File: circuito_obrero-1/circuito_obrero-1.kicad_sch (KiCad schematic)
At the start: 37 parts, among them J1 Conn_01x03_Pin, J10 Conn_01x05, J2 Conn_01x03_Pin, J3 Conn_01x03_Pin, J4 Conn_01x03_Pin, J5 Conn_01x03_Pin, J6 Conn_01x03_Pin, J7 Conn_01x03_Pin, J8 Conn_01x03_Pin, J9 Conn_01x05, U1 74HC165, U2 74HC165, U3 74HC165

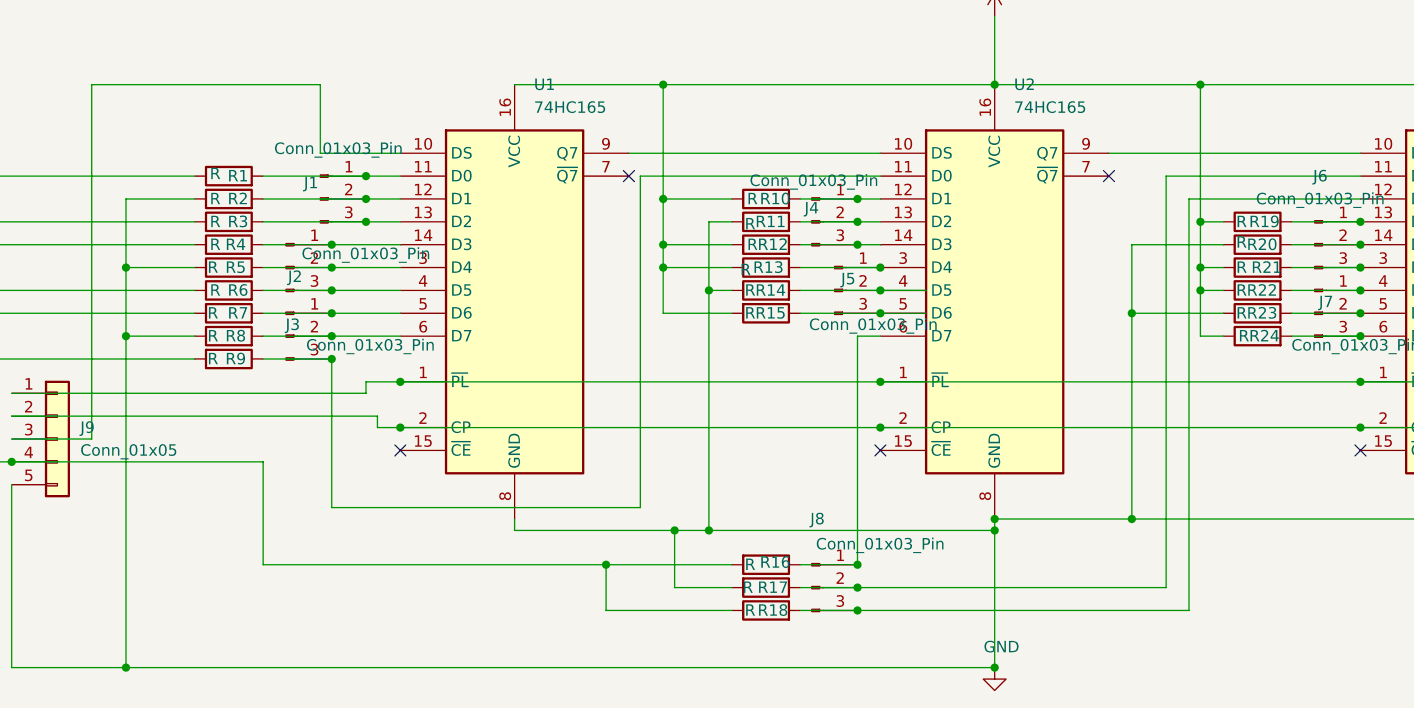
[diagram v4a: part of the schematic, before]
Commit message: revision de resistencias y otros elementos: falta ruteo en el circuito
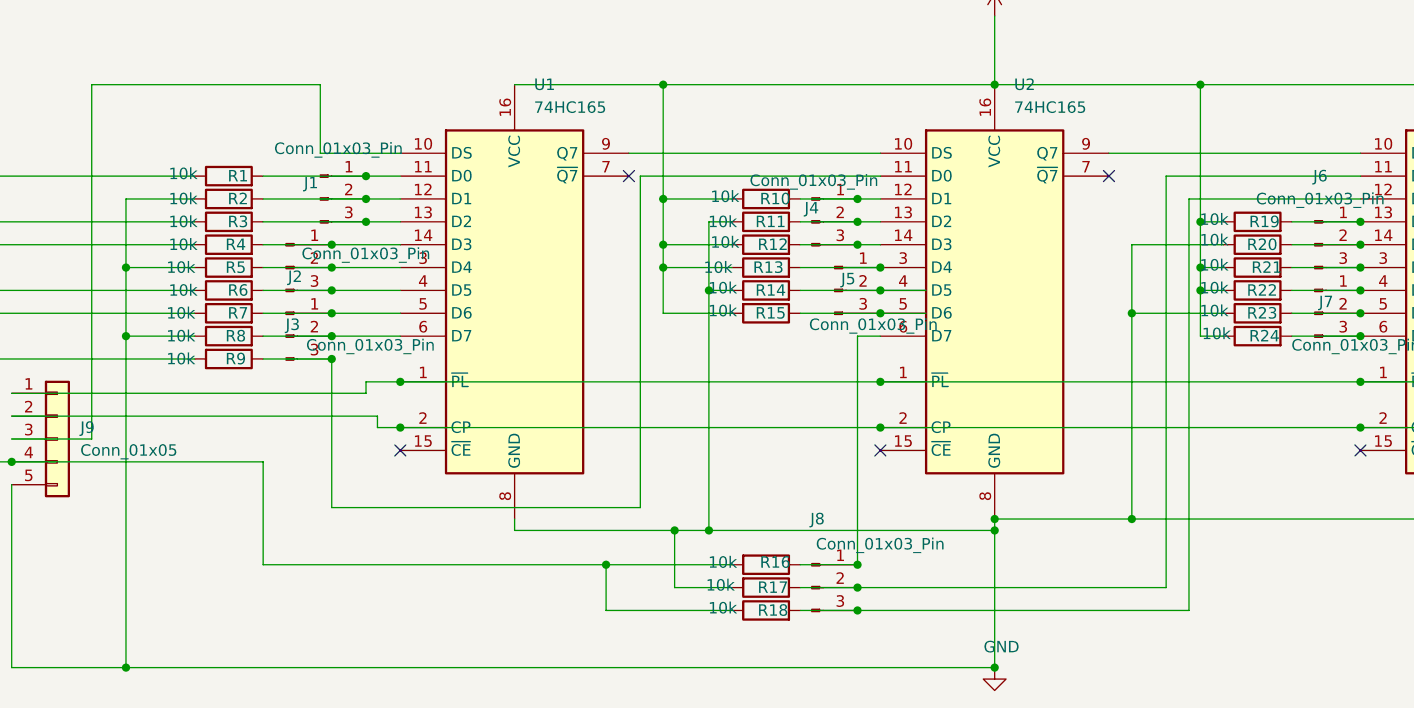
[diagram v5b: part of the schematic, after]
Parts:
- R1, R10, R11, R12, R13, R14, R15, R16, R17, R18, R19, R2, R20, R21, R22, R23, R24, R3, R4, R5, R6, R7, R8, R9: value R -> 10k; footprint Resistor_THT:R_Axial_DIN0204_L3.6mm_D1.6mm_P5.08mm_Horizontal -> Resistor_THT:R_Axial_DIN0204_L3.6mm_D1.6mm_P7.62mm_Horizontal
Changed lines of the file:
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@@
 			)
 		)
-		(property "Value" "R"
-			(at 127.762 100.33 90)
+		(property "Value" "10k"
+			(at 124.714 100.076 90)
 			(show_name no)
 			(do_not_autoplace no)
@@
 			)
 		)
-		(property "Footprint" "Resistor_THT:R_Axial_DIN0204_L3.6mm_D1.6mm_P5.08mm_Horizontal"
+		(property "Footprint" "Resistor_THT:R_Axial_DIN0204_L3.6mm_D1.6mm_P7.62mm_Horizontal"
 			(at 129.54 98.552 90)
 			(hide yes)
@@
 			)
 		)
-		(property "Value" "R"
-			(at 68.326 90.17 90)
+		(property "Value" "10k"
+			(at 64.77 90.17 90)
 			(show_name no)
 			(do_not_autoplace no)
@@
 			)
 		)
-		(property "Footprint" "Resistor_THT:R_Axial_DIN0204_L3.6mm_D1.6mm_P5.08mm_Horizontal"
+		(property "Footprint" "Resistor_THT:R_Axial_DIN0204_L3.6mm_D1.6mm_P7.62mm_Horizontal"
 			(at 69.85 91.948 90)
 			(hide yes)
@@
 			)
 		)
-		(property "Value" "R"
-			(at 128.016 87.63 90)
+		(property "Value" "10k"
+			(at 124.968 87.376 90)
 			(show_name no)
 			(do_not_autoplace no)
@@
 			)
 		)
-		(property "Footprint" "Resistor_THT:R_Axial_DIN0204_L3.6mm_D1.6mm_P5.08mm_Horizontal"
+		(property "Footprint" "Resistor_THT:R_Axial_DIN0204_L3.6mm_D1.6mm_P7.62mm_Horizontal"
 			(at 129.54 89.408 90)
 			(hide yes)
@@
 			)
 		)
-		(property "Value" "R"
-			(at 182.372 90.17 90)
+		(property "Value" "10k"
+			(at 179.324 89.916 90)
 			(show_name no)
 			(do_not_autoplace no)
@@
 			)
 		)
-		(property "Footprint" "Resistor_THT:R_Axial_DIN0204_L3.6mm_D1.6mm_P5.08mm_Horizontal"
+		(property "Footprint" "Resistor_THT:R_Axial_DIN0204_L3.6mm_D1.6mm_P7.62mm_Horizontal"
 			(at 184.15 91.948 90)
 			(hide yes)
@@
 			)
 		)
-		(property "Value" "R"
-			(at 182.372 95.25 90)
+		(property "Value" "10k"
+			(at 179.324 94.996 90)
 			(show_name no)
 			(do_not_autoplace no)
@@
 			)
 		)
-		(property "Footprint" "Resistor_THT:R_Axial_DIN0204_L3.6mm_D1.6mm_P5.08mm_Horizontal"
+		(property "Footprint" "Resistor_THT:R_Axial_DIN0204_L3.6mm_D1.6mm_P7.62mm_Horizontal"
 			(at 184.15 97.028 90)
 			(hide yes)
@@
 			)
 		)
-		(property "Value" "R"
-			(at 68.326 92.71 90)
+		(property "Value" "10k"
+			(at 64.77 92.71 90)
 			(show_name no)
 			(do_not_autoplace no)
@@
 			)
 		)
-		(property "Footprint" "Resistor_THT:R_Axial_DIN0204_L3.6mm_D1.6mm_P5.08mm_Horizontal"
+		(property "Footprint" "Resistor_THT:R_Axial_DIN0204_L3.6mm_D1.6mm_P7.62mm_Horizontal"
 			(at 69.85 94.488 90)
 			(hide yes)
@@
 			)
 		)
-		(property "Value" "R"
-			(at 182.626 102.87 90)
+		(property "Value" "10k"
+			(at 179.578 102.616 90)
 			(show_name no)
 			(do_not_autoplace no)
@@
 			)
 		)
-		(property "Footprint" "Resistor_THT:R_Axial_DIN0204_L3.6mm_D1.6mm_P5.08mm_Horizontal"
+		(property "Footprint" "Resistor_THT:R_Axial_DIN0204_L3.6mm_D1.6mm_P7.62mm_Horizontal"
 			(at 184.15 104.648 90)
 			(hide yes)
@@
 			)
 		)
-		(property "Value" "R"
-			(at 128.016 92.71 90)
+		(property "Value" "10k"
+			(at 124.968 92.456 90)
 			(show_name no)
 			(do_not_autoplace no)
@@
 			)
 		)
-		(property "Footprint" "Resistor_THT:R_Axial_DIN0204_L3.6mm_D1.6mm_P5.08mm_Horizontal"
+		(property "Footprint" "Resistor_THT:R_Axial_DIN0204_L3.6mm_D1.6mm_P7.62mm_Horizontal"
 			(at 129.54 94.488 90)
 			(hide yes)
@@
 			)
 		)
-		(property "Value" "R"
-			(at 68.072 95.25 90)
+		(property "Value" "10k"
+			(at 64.516 95.25 90)
 			(show_name no)
 			(do_not_autoplace no)
@@
 			)
 		)
-		(property "Footprint" "Resistor_THT:R_Axial_DIN0204_L3.6mm_D1.6mm_P5.08mm_Horizontal"
+		(property "Footprint" "Resistor_THT:R_Axial_DIN0204_L3.6mm_D1.6mm_P7.62mm_Horizontal"
 			(at 69.85 97.028 90)
 			(hide yes)
@@
 			)
 		)
-		(property "Value" "R"
-			(at 182.372 100.33 90)
+		(property "Value" "10k"
+			(at 179.324 100.076 90)
 			(show_name no)
 			(do_not_autoplace no)
@@
 			)
 		)
-		(property "Footprint" "Resistor_THT:R_Axial_DIN0204_L3.6mm_D1.6mm_P5.08mm_Horizontal"
+		(property "Footprint" "Resistor_THT:R_Axial_DIN0204_L3.6mm_D1.6mm_P7.62mm_Horizontal"
 			(at 184.15 102.108 90)
 			(hide yes)
@@
 			)
 		)
-		(property "Value" "R"
-			(at 127.254 95.504 90)
+		(property "Value" "10k"
+			(at 124.206 95.25 90)
 			(show_name no)
 			(do_not_autoplace no)
@@
 			)
 		)
-		(property "Footprint" "Resistor_THT:R_Axial_DIN0204_L3.6mm_D1.6mm_P5.08mm_Horizontal"
+		(property "Footprint" "Resistor_THT:R_Axial_DIN0204_L3.6mm_D1.6mm_P7.62mm_Horizontal"
 			(at 129.54 97.028 90)
 			(hide yes)
@@
 			)
 		)
-		(property "Value" "R"
-			(at 127.762 133.35 90)
+		(property "Value" "10k"
+			(at 124.714 133.096 90)
 			(show_name no)
 			(do_not_autoplace no)
@@
 			)
 		)
-		(property "Footprint" "Resistor_THT:R_Axial_DIN0204_L3.6mm_D1.6mm_P5.08mm_Horizontal"
+		(property "Footprint" "Resistor_THT:R_Axial_DIN0204_L3.6mm_D1.6mm_P7.62mm_Horizontal"
 			(at 129.54 135.128 90)
 			(hide yes)
@@
 			)
 		)
-		(property "Value" "R"
-			(at 68.072 105.41 90)
+		(property "Value" "10k"
+			(at 64.516 105.41 90)
 			(show_name no)
 			(do_not_autoplace no)
@@
 			)
 		)
-		(property "Footprint" "Resistor_THT:R_Axial_DIN0204_L3.6mm_D1.6mm_P5.08mm_Horizontal"
+		(property "Footprint" "Resistor_THT:R_Axial_DIN0204_L3.6mm_D1.6mm_P7.62mm_Horizontal"
 			(at 69.85 103.632 90)
 			(hide yes)
@@
 			)
 		)
-		(property "Value" "R"
-			(at 68.326 97.79 90)
+		(property "Value" "10k"
+			(at 64.77 97.79 90)
 			(show_name no)
 			(do_not_autoplace no)
@@
 			)
 		)
-		(property "Footprint" "Resistor_THT:R_Axial_DIN0204_L3.6mm_D1.6mm_P5.08mm_Horizontal"
+		(property "Footprint" "Resistor_THT:R_Axial_DIN0204_L3.6mm_D1.6mm_P7.62mm_Horizontal"
 			(at 69.85 99.568 90)
 			(hide yes)
@@
 			)
 		)
-		(property "Value" "R"
-			(at 127.762 128.27 90)
+		(property "Value" "10k"
+			(at 124.714 128.016 90)
 			(show_name no)
 			(do_not_autoplace no)
@@
 			)
 		)
-		(property "Footprint" "Resistor_THT:R_Axial_DIN0204_L3.6mm_D1.6mm_P5.08mm_Horizontal"
+		(property "Footprint" "Resistor_THT:R_Axial_DIN0204_L3.6mm_D1.6mm_P7.62mm_Horizontal"
 			(at 129.54 126.492 90)
 			(hide yes)
@@
 			)
 		)
-		(property "Value" "R"
-			(at 182.372 92.456 90)
+		(property "Value" "10k"
+			(at 179.324 92.202 90)
 			(show_name no)
 			(do_not_autoplace no)
@@
 			)
 		)
-		(property "Footprint" "Resistor_THT:R_Axial_DIN0204_L3.6mm_D1.6mm_P5.08mm_Horizontal"
+		(property "Footprint" "Resistor_THT:R_Axial_DIN0204_L3.6mm_D1.6mm_P7.62mm_Horizontal"
 			(at 184.15 94.488 90)
 			(hide yes)
@@
 			)
 		)
-		(property "Value" "R"
-			(at 68.072 102.87 90)
+		(property "Value" "10k"
+			(at 64.516 102.87 90)
 			(show_name no)
 			(do_not_autoplace no)
@@
 			)
 		)
-		(property "Footprint" "Resistor_THT:R_Axial_DIN0204_L3.6mm_D1.6mm_P5.08mm_Horizontal"
+		(property "Footprint" "Resistor_THT:R_Axial_DIN0204_L3.6mm_D1.6mm_P7.62mm_Horizontal"
 			(at 69.85 104.648 90)
 			(hide yes)
@@
 			)
 		)
-		(property "Value" "R"
-			(at 68.072 100.33 90)
+		(property "Value" "10k"
+			(at 64.516 100.33 90)
 			(show_name no)
 			(do_not_autoplace no)
@@
 			)
 		)
-		(property "Footprint" "Resistor_THT:R_Axial_DIN0204_L3.6mm_D1.6mm_P5.08mm_Horizontal"
+		(property "Footprint" "Resistor_THT:R_Axial_DIN0204_L3.6mm_D1.6mm_P7.62mm_Horizontal"
 			(at 69.85 102.108 90)
 			(hide yes)
@@
 			)
 		)
-		(property "Value" "R"
-			(at 182.372 97.79 90)
+		(property "Value" "10k"
+			(at 179.324 97.536 90)
 			(show_name no)
 			(do_not_autoplace no)
@@
 			)
 		)
-		(property "Footprint" "Resistor_THT:R_Axial_DIN0204_L3.6mm_D1.6mm_P5.08mm_Horizontal"
+		(property "Footprint" "Resistor_THT:R_Axial_DIN0204_L3.6mm_D1.6mm_P7.62mm_Horizontal"
 			(at 184.15 99.568 90)
 			(hide yes)
@@
 			)
 		)
-		(property "Value" "R"
-			(at 127.762 97.79 90)
+		(property "Value" "10k"
+			(at 124.714 97.536 90)
 			(show_name no)
 			(do_not_autoplace no)
@@
 			)
 		)
-		(property "Footprint" "Resistor_THT:R_Axial_DIN0204_L3.6mm_D1.6mm_P5.08mm_Horizontal"
+		(property "Footprint" "Resistor_THT:R_Axial_DIN0204_L3.6mm_D1.6mm_P7.62mm_Horizontal"
 			(at 129.54 99.568 90)
 			(hide yes)
@@
 			)
 		)
-		(property "Value" "R"
-			(at 68.326 87.63 90)
+		(property "Value" "10k"
+			(at 64.77 87.63 90)
 			(show_name no)
 			(do_not_autoplace no)
@@
 			)
 		)
-		(property "Footprint" "Resistor_THT:R_Axial_DIN0204_L3.6mm_D1.6mm_P5.08mm_Horizontal"
+		(property "Footprint" "Resistor_THT:R_Axial_DIN0204_L3.6mm_D1.6mm_P7.62mm_Horizontal"
 			(at 69.85 89.408 90)
 			(hide yes)
@@
 			)
 		)
-		(property "Value" "R"
-			(at 68.326 84.836 90)
+		(property "Value" "10k"
+			(at 64.77 84.836 90)
 			(show_name no)
 			(do_not_autoplace no)
@@
 			)
 		)
-		(property "Footprint" "Resistor_THT:R_Axial_DIN0204_L3.6mm_D1.6mm_P5.08mm_Horizontal"
+		(property "Footprint" "Resistor_THT:R_Axial_DIN0204_L3.6mm_D1.6mm_P7.62mm_Horizontal"
 			(at 69.85 86.868 90)
 			(hide yes)
@@
 			)
 		)
-		(property "Value" "R"
-			(at 127.508 130.81 90)
+		(property "Value" "10k"
+			(at 124.46 130.556 90)
 			(show_name no)
 			(do_not_autoplace no)
@@
 			)
 		)
-		(property "Footprint" "Resistor_THT:R_Axial_DIN0204_L3.6mm_D1.6mm_P5.08mm_Horizontal"
+		(property "Footprint" "Resistor_THT:R_Axial_DIN0204_L3.6mm_D1.6mm_P7.62mm_Horizontal"
 			(at 129.54 129.032 90)
 			(hide yes)
@@
 			)
 		)
-		(property "Value" "R"
-			(at 127.762 90.424 90)
+		(property "Value" "10k"
+			(at 124.714 90.17 90)
 			(show_name no)
 			(do_not_autoplace no)
@@
 			)
 		)
-		(property "Footprint" "Resistor_THT:R_Axial_DIN0204_L3.6mm_D1.6mm_P5.08mm_Horizontal"
+		(property "Footprint" "Resistor_THT:R_Axial_DIN0204_L3.6mm_D1.6mm_P7.62mm_Horizontal"
 			(at 129.54 91.948 90)
 			(hide yes)

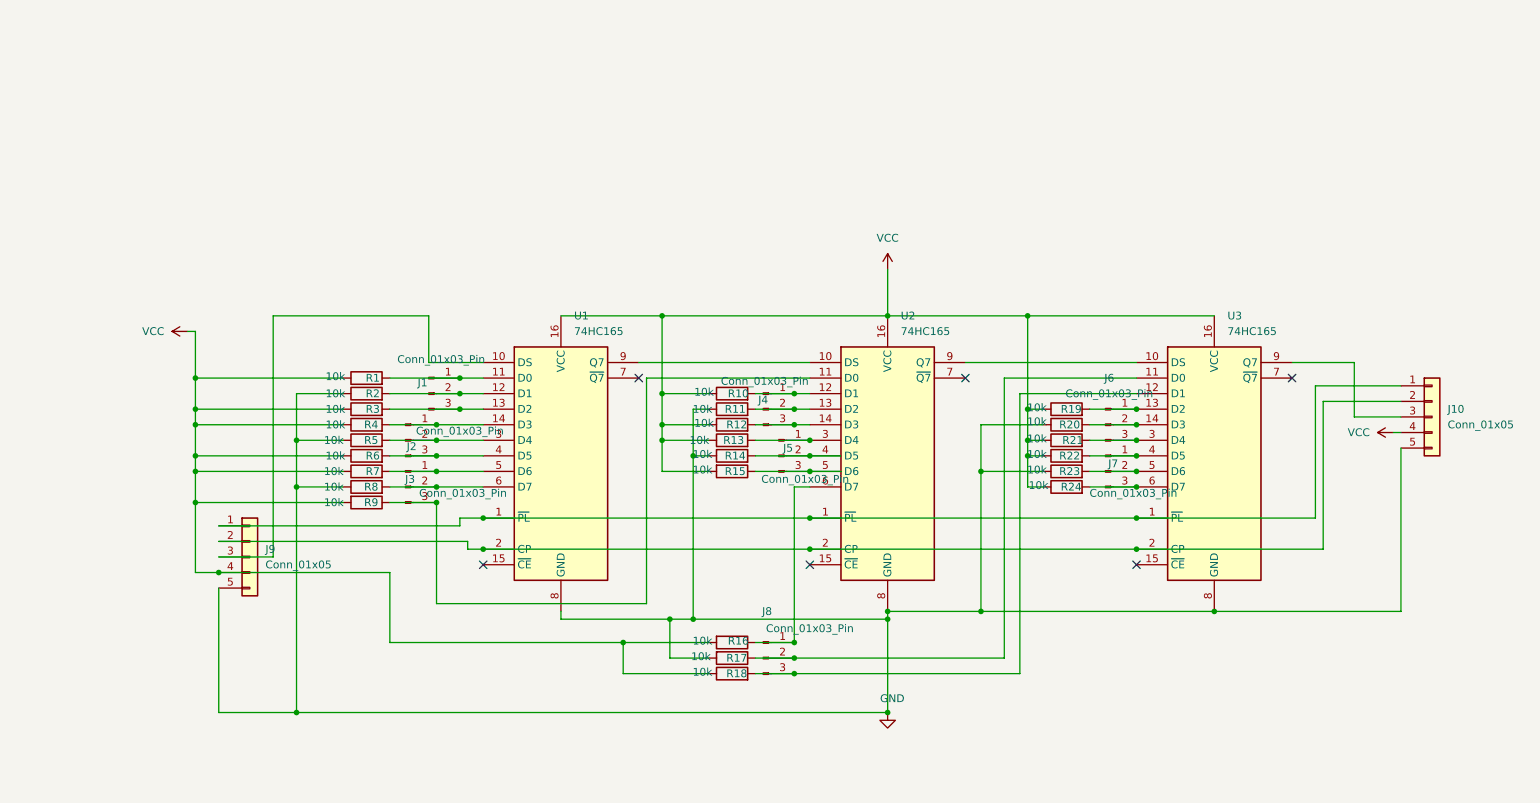
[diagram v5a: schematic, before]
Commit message: preruteo: revisar y optimizar
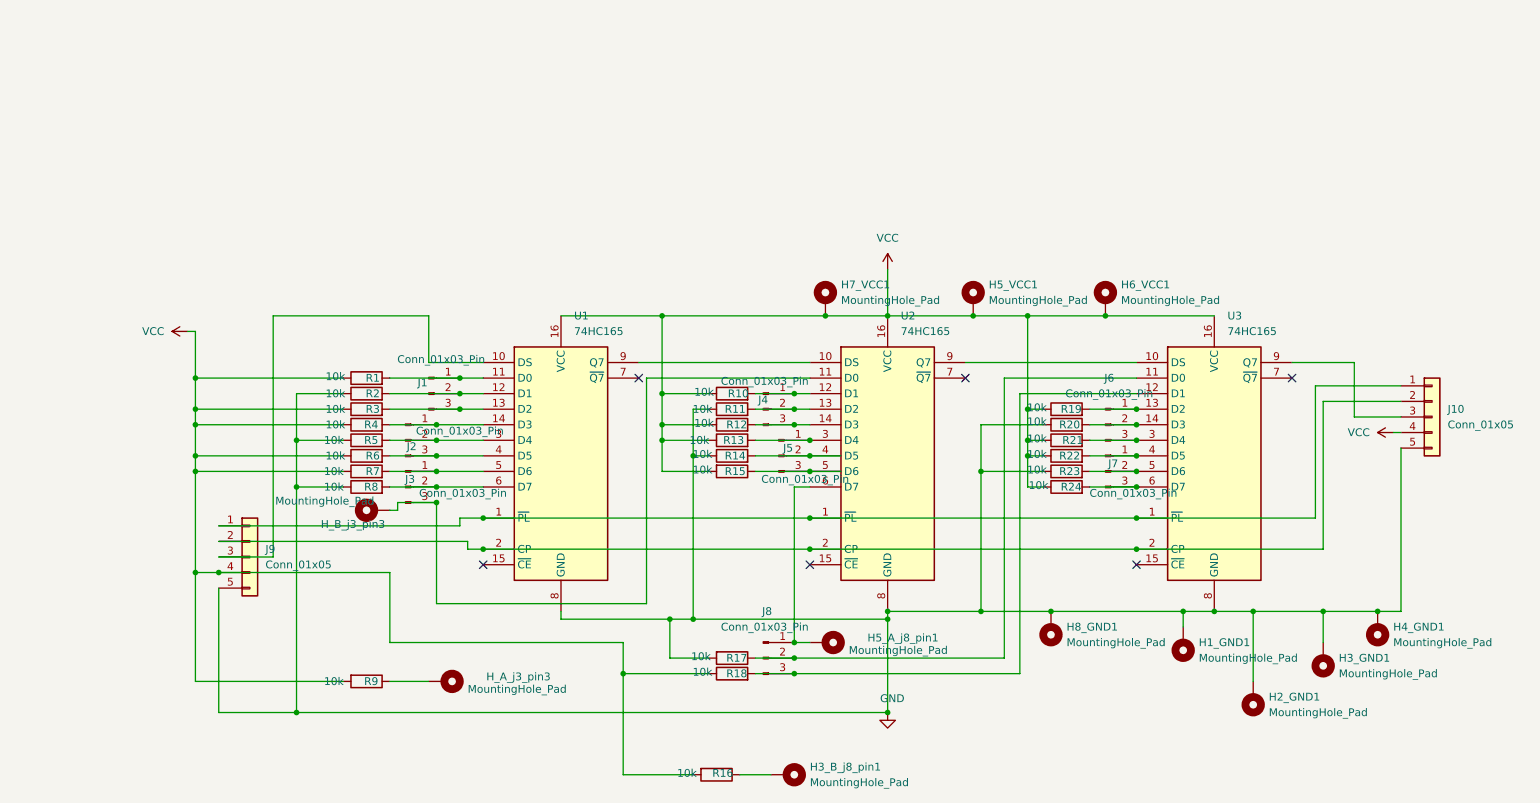
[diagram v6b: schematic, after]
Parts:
- added H1_GND1, H2_GND1, H3_B_j8_pin1, H3_GND1, H4_GND1, H5_A_j8_pin1, H5_VCC1, H6_VCC1, H7_VCC1, H8_GND1, H_A_j3_pin3, H_B_j3_pin3: MountingHole_Pad, MountingHole:MountingHole_2.2mm_M2_DIN965_Pad_TopOnly, symbol Mechanical:MountingHole_Pad
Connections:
- net GND: now also H1_GND1.1, H2_GND1.1, H3_GND1.1, H4_GND1.1, H8_GND1.1
- net VCC: now also H5_VCC1.1, H6_VCC1.1, H7_VCC1.1
- net at J3.3 (Pin_3), U2.11 (D0): now also H_B_j3_pin3.1; no longer R9.1
- net at J8.1 (Pin_1), U2.6 (D7): now also H5_A_j8_pin1.1; no longer R16.1
- new net: H_A_j3_pin3.1, R9.1
- new net: H3_B_j8_pin1.1, R16.1
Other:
- moved on the sheet: R16, R9

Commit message: probando rerutear
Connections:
- net at H5_A_j8_pin1.1, J8.1 (Pin_1), U2.6 (D7): now also H3_B_j8_pin1.1, R16.1
- net at H_B_j3_pin3.1, J3.3 (Pin_3), U2.11 (D0): now also H_A_j3_pin3.1, R9.1
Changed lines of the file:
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@@
+	)
+	(junction
+		(at 142.24 128.27)
+		(diameter 0)
+		(color 0 0 0 0)
 	)
 	(junction
@@
 	)
 	(junction
+		(at 74.93 106.68)
+		(diameter 0)
+		(color 0 0 0 0)
+	)
+	(junction
+		(at 80.01 134.62)
+		(diameter 0)
+		(color 0 0 0 0)
+	)
+	(junction
 		(at 139.7 87.63)
 		(diameter 0)
@@
 	(junction
 		(at 85.09 87.63)
+		(diameter 0)
+		(color 0 0 0 0)
+	)
+	(junction
+		(at 135.89 149.86)
 		(diameter 0)
 		(color 0 0 0 0)
@@
 	(wire
 		(pts
+			(xy 74.93 106.68) (xy 74.93 132.08)
+		)
+		(stroke
+			(width 0)
+			(type default)
+		)
+	)
+	(wire
+		(pts
 			(xy 66.04 87.63) (xy 58.42 87.63)
 		)
@@
 	(wire
 		(pts
+			(xy 142.24 128.27) (xy 142.24 146.05)
+		)
+		(stroke
+			(width 0)
+			(type default)
+		)
+	)
+	(wire
+		(pts
 			(xy 118.11 92.71) (xy 118.11 87.63)
 		)
@@
 	(wire
 		(pts
+			(xy 80.01 132.08) (xy 80.01 134.62)
+		)
+		(stroke
+			(width 0)
+			(type default)
+		)
+	)
+	(wire
+		(pts
 			(xy 177.8 95.25) (xy 177.8 90.17)
 		)
@@
 	(wire
 		(pts
+			(xy 135.89 146.05) (xy 135.89 149.86)
+		)
+		(stroke
+			(width 0)
+			(type default)
+		)
+	)
+	(wire
+		(pts
+			(xy 142.24 146.05) (xy 135.89 146.05)
+		)
+		(stroke
+			(width 0)
+			(type default)
+		)
+	)
+	(wire
+		(pts
 			(xy 41.91 116.84) (xy 45.72 116.84)
 		)
@@
 		)
 		(stroke
+			(width 0)
+			(type default)
+		)
+	)
+	(wire
+		(pts
+			(xy 74.93 132.08) (xy 80.01 132.08)
+		)
+		(stroke
